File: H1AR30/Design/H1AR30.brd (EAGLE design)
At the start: 34.6 x 30 mm, 21 parts, among them P1 HEXABIT_17.32_NO_P3, U1 STM32F091CBU6, X1 XTALL_CSTCE8M00G52

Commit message: in this commit: - schematic is done - PCB is done - all output files were generated
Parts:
- added C10: 4.7uF, Hexabitz:C-0805-POL
- added C11, C12, C15: 100nF, Hexabitz:C-0603
- added C13, C14: 47pF, Hexabitz:C-0603
- added C16: 100uF, Hexabitz:C-3225
- added C17: 1uF, Hexabitz:C-0805-POL
- added D2: RED, Hexabitz:VLMS1300-GS08
- added D3: GREEN, Hexabitz:VLMS1300-GS08
- added FB2: (no value), Hexabitz:FB-TDK_MMZ1608Y300B
- added PWR: 3-644456-2, Hexabitz:TE_3-644456-2
- added R4, R5: 27.0Ω, Hexabitz:R-0603
- added R6: 39.0Ω, Hexabitz:R-0603
- added R7: 270.0Ω, Hexabitz:R-0603
- added R8: 4.7kΩ, Hexabitz:R-0603
- added R9: 10kΩ, Hexabitz:R-0603
- added U2: FT230XQ-R, Hexabitz:QFN16
- added U3: LM3940IMP-3.3, Hexabitz:SOT230P696X180-4N
- added USB-B*: 1981568-1, Hexabitz:TE_1981568-1
- C1: value 10nF -> 100nF
- C3: value 100nF -> 4.7uF; device Hexabitz:C-0603 -> Hexabitz:C-0805-POL
- C5: value 100nF -> 10nF
- C7: value 4.7uF -> 100nF; device Hexabitz:C-0805-POL -> Hexabitz:C-0603
- D1: value VLMS1300-GS08 -> RED
- R2: value 0.0R -> 10.0K
- R3: value 10.0K -> 0.0R
- moved C6 15.3 mm to (29.0, 45.0), turned to 90 degrees
- moved C8 14.5 mm to (28.7, 37.9)
- moved C7 13.8 mm to (39.6, 46.4), turned to 180 degrees
- moved D1 13.0 mm to (38.2, 31.2), turned to 180 degrees
- moved R1 12.5 mm to (36.7, 31.3)
- moved R2 12.1 mm to (39.8, 45.4), flipped to the top, turned to 180 degrees
- moved C3 11.5 mm to (26.9, 45.1)
- moved C5 10.5 mm to (40.0, 37.4)
- moved D 10.5 mm to (23.0, 34.7)
- moved C 10.5 mm to (23.0, 37.3)
- moved R3 9.42 mm to (44.1, 37.4), turned to 90 degrees
- moved C1 8.43 mm to (47.0, 37.4), turned to 180 degrees
- moved R 8.11 mm to (46.3, 35.3)
- moved U1 6.35 mm to (33.6, 40.9)
- moved X1 5.87 mm to (40.5, 41.3)
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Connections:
- new net N$1: R1.2, U1.P$16
- new net N$10: FB2.2, PWR.2
- new net N$11: C17.1, FB2.1, U3.1
- new net N$12: R5.2, U2.6
- new net N$13: R4.2, U2.7
- new net N$14: R7.1, U2.5
- new net N$15: R6.1, U2.11
- new net N$16: D2.C, R7.2
- new net N$17: D3.C, R6.2
- new net N$18: PWR.1, R8.2, USB-B*.1
- new net N$2: C14.1, R4.1, USB-B*.2
- new net UART1_CTS: U1.P$32, U2.16
- new net UART1_RTS: U1.P$33, U2.4
- new net VBUS_SENSE: R8.1, R9.2, U2.14
- net B1: now also R2.2; no longer R3.2
- net GND: now also C1.2, C10.2, C11.2, C12.2, C13.2, C14.2, C15.2, C16.1, C17.2, R9.1, U1.P$19, U1.P$27, U1.P$3, U1.P$38, U2.13, U2.17, U2.3, U3.2, U3.4, USB-B*.10, USB-B*.11, USB-B*.5, USB-B*.6, USB-B*.7, USB-B*.8, USB-B*.9; no longer C5.2
- net N$3: now also C13.1, R5.1, USB-B*.3; no longer R1.2, U1.P$32
- net R1: now also C1.1; no longer C8.1
- net UART1_RX: now also U2.15
- net UART1_TX: now also U2.2
- net UART2_RX: now also P1.PAD_PD1
- net UART2_TX: now also P1.PAD_PU1
- net UART3_RX: now also P1.PAD_PD4
- net UART3_TX: now also P1.PAD_PU4
- net UART4_RX: now also P1.PAD_PD5
- net UART4_TX: now also P1.PAD_PU5
- net UART5_RX: now also P1.PAD_PD6
- net UART5_TX: now also P1.PAD_PU6
- net UART6_RX: now also P1.PAD_PD2
- net UART6_TX: now also P1.PAD_PU2
- net VDD: now also C10.1, C11.1, C12.1, C15.1, C16.2, C8.1, D2.A, D3.A, U2.1, U2.10, U2.8, U2.9, U3.3; no longer C5.1
- net VDDA: now also C5.1; no longer C1.1
- net VSSA: now also C5.2, R3.2; no longer C1.2, R2.2
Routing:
- net GND: track 0.00 -> 58.8 mm, vias 0 -> 6
- net VDD: track 0.00 -> 54.1 mm, vias 0 -> 6
- net UART4_RX: track 0.00 -> 26.8 mm, vias 0 -> 2
- net UART4_TX: track 0.00 -> 23.8 mm, vias 0 -> 1
- net UART1_CTS: track 0.00 -> 19.3 mm, vias 0 -> 2
- net UART6_TX: track 0.00 -> 18.7 mm, vias 0 -> 1
- net UART6_RX: track 0.00 -> 18.4 mm
- net UART1_RX: track 0.00 -> 18.2 mm, vias 0 -> 2
- net UART3_TX: track 0.00 -> 17.9 mm, vias 0 -> 1
- net UART3_RX: track 0.00 -> 17.2 mm, vias 0 -> 2
- net N$9: track 0.00 -> 17.1 mm, vias 0 -> 2
- net UART1_RTS: track 0.00 -> 17.1 mm, vias 0 -> 2
- net N$7: track 0.00 -> 15.5 mm, vias 0 -> 1
- net UART1_TX: track 0.00 -> 14.9 mm, vias 0 -> 2
- net UART2_RX: track 0.00 -> 14.8 mm, vias 0 -> 2
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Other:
- board text added: "H1AR20"
- board text removed: "H1AR30"

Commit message: replaced (USB-B*) with (PUSB*) and fixed gerber files
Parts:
- renumbered USB-B* to PUSB*
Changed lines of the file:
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@@
 <drawing>
 <settings>
-<setting alwaysvectorfont="yes"/>
+<setting alwaysvectorfont="no"/>
 <setting verticaltext="up"/>
 </settings>
@@
 <attribute name="VALUE" x="30.8704" y="35.36611875" size="1.016" layer="27" ratio="10" rot="SR0"/>
 </element>
-<element name="USB-B*" library="Hexabitz" package="TE_1981568-1" value="1981568-1" x="34.8615" y="22.7838" smashed="yes">
+<element name="PUSB*" library="Hexabitz" package="TE_1981568-1" value="1981568-1" x="34.8615" y="22.7838" smashed="yes">
 <attribute name="DESCRIPTION" value=" USB - micro B USB 2.0 Receptacle Connector 5 Position Surface Mount, Right Angle " x="34.8615" y="22.7838" size="1.778" layer="27" display="off"/>
 <attribute name="MFN" value="TE Connectivity" x="34.8615" y="22.7838" size="1.778" layer="27" display="off"/>
@@
 <wire x1="33.6644625" y1="40.0685" x2="31.544" y2="42.1889625" width="0.254" layer="1"/>
 <wire x1="31.544" y1="42.9641" x2="31.544" y2="42.1889625" width="0.254" layer="1"/>
-<contactref element="USB-B*" pad="5"/>
-<contactref element="USB-B*" pad="11"/>
-<contactref element="USB-B*" pad="6"/>
-<contactref element="USB-B*" pad="10"/>
-<contactref element="USB-B*" pad="7"/>
-<contactref element="USB-B*" pad="9"/>
-<contactref element="USB-B*" pad="8"/>
+<contactref element="PUSB*" pad="5"/>
+<contactref element="PUSB*" pad="11"/>
+<contactref element="PUSB*" pad="6"/>
+<contactref element="PUSB*" pad="10"/>
+<contactref element="PUSB*" pad="7"/>
+<contactref element="PUSB*" pad="9"/>
+<contactref element="PUSB*" pad="8"/>
 <wire x1="36.1615" y1="25.4588" x2="37.8365" y2="25.4588" width="0.254" layer="1"/>
 <wire x1="37.8365" y1="25.4588" x2="38.0615" y2="25.2338" width="0.254" layer="1"/>
@@
 <contactref element="C14" pad="1"/>
 <contactref element="R4" pad="1"/>
-<contactref element="USB-B*" pad="2"/>
+<contactref element="PUSB*" pad="2"/>
 <wire x1="33.4645" y1="22.1352" x2="33.4527" y2="22.147" width="0.254" layer="16"/>
 <wire x1="33.4527" y1="22.147" x2="33.4527" y2="23.8887" width="0.254" layer="16"/>
@@
 <contactref element="R5" pad="1"/>
 <wire x1="36.9706" y1="22.3647" x2="36.9824" y2="22.3765" width="0.254" layer="16"/>
-<contactref element="USB-B*" pad="3"/>
+<contactref element="PUSB*" pad="3"/>
 <wire x1="39.7256" y1="23.5994" x2="39.2585" y2="24.0665" width="0.254" layer="1"/>
 <via x="39.7256" y="23.5994" extent="1-16" drill="0.35"/>
@@
 <wire x1="28.321" y1="30.353" x2="27.1272" y2="31.5468" width="0.254" layer="16"/>
 <wire x1="27.1272" y1="31.5468" x2="27.1272" y2="32.0675" width="0.254" layer="16"/>
-<contactref element="USB-B*" pad="1"/>
+<contactref element="PUSB*" pad="1"/>
 <wire x1="33.5615" y1="25.4588" x2="33.5615" y2="27.8176" width="0.254" layer="1"/>
 <wire x1="32.8284" y1="28.5507" x2="32.0929" y2="28.5507" width="0.254" layer="1"/>

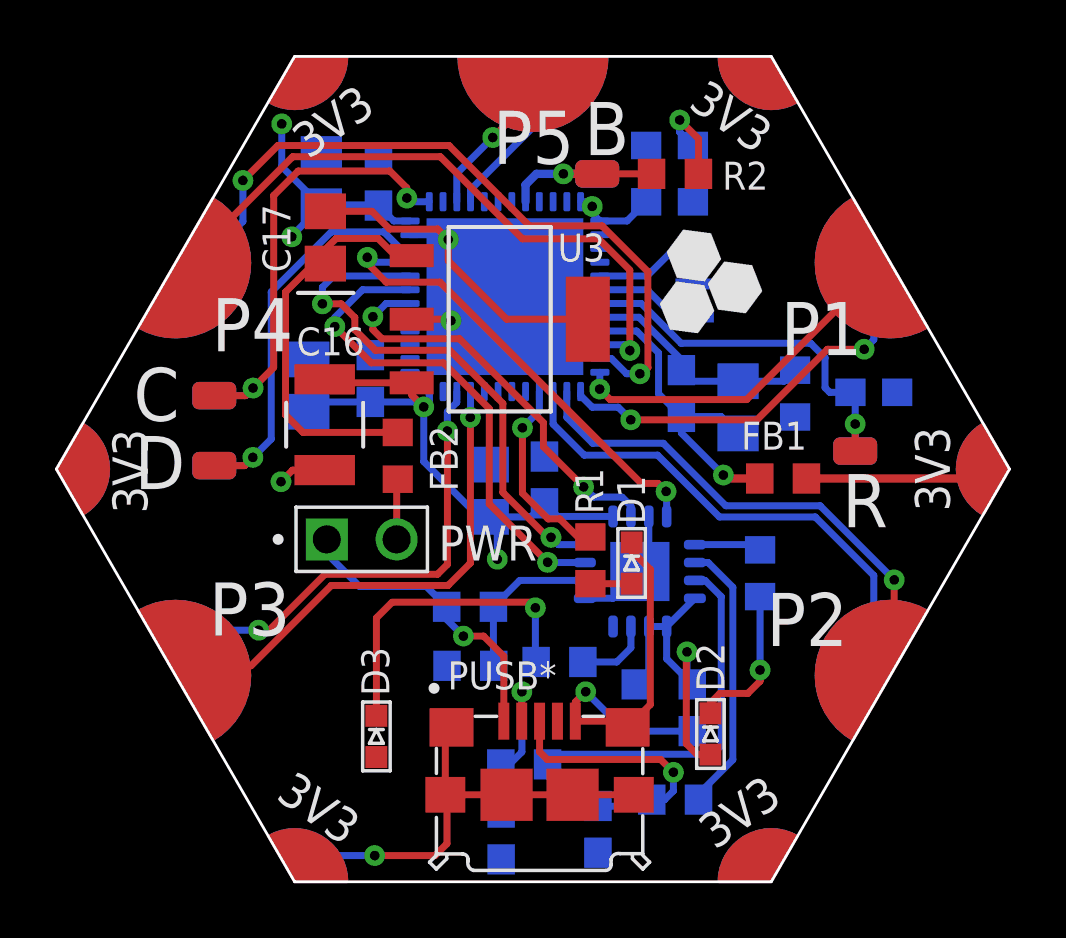
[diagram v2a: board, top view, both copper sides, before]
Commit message: Fix PN and move it a bit. Minor trace update Regenerate gerber and pick n place
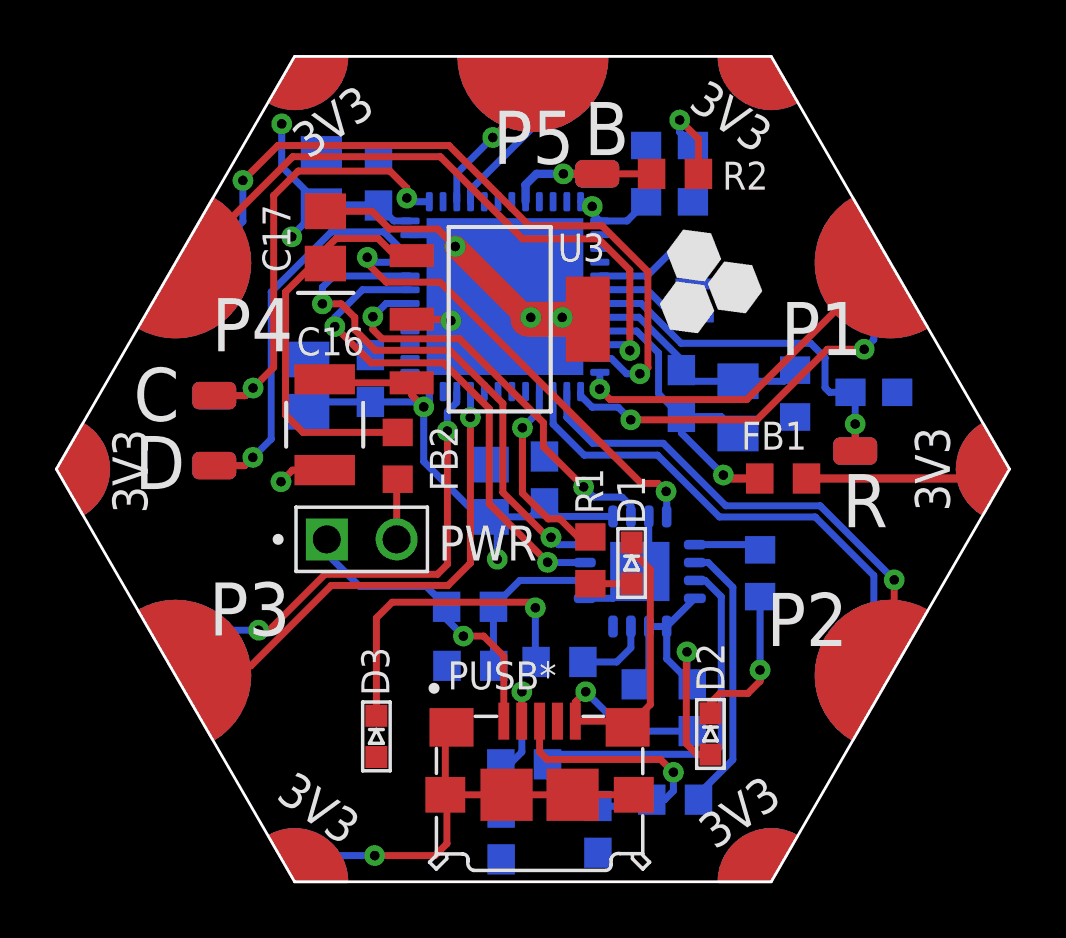
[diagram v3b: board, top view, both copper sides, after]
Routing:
- net GND: track 58.8 -> 58.4 mm, vias 6 -> 8
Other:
- board text added: "H1AR30"
- board text removed: "H1AR20"
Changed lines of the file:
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@@
 <drawing>
 <settings>
-<setting alwaysvectorfont="no"/>
+<setting alwaysvectorfont="yes"/>
 <setting verticaltext="up"/>
 </settings>
-<grid distance="0.5" unitdist="mil" unit="mil" style="lines" multiple="1" display="yes" altdistance="5" altunitdist="mil" altunit="mil"/>
+<grid distance="5" unitdist="mil" unit="mil" style="lines" multiple="1" display="yes" altdistance="5" altunitdist="mil" altunit="mil"/>
 <layers>
 <layer number="1" name="Top" color="4" fill="1" visible="yes" active="yes"/>
@@
 <text x="34.6454" y="46.6784" size="1.9304" layer="21" font="vector" align="center">P5</text>
 <text x="34.5311" y="46.6911" size="1.9304" layer="22" font="vector" rot="MR0" align="center">P5</text>
-<text x="28.2194" y="24.106125" size="1.6764" layer="22" font="vector" rot="MR0" align="center">H1AR20</text>
+<text x="28.1813" y="25.299925" size="1.6764" layer="22" font="vector" rot="MR0" align="center">H1AR30</text>
 <rectangle x1="40.60316875" y1="39.551103125" x2="40.6179" y2="39.565834375" layer="21"/>
 <rectangle x1="40.485315625" y1="39.565834375" x2="40.632634375" y2="39.580565625" layer="21"/>
@@
 <wire x1="28.768" y1="43.9903" x2="29.4132" y2="43.3451" width="0.254" layer="1"/>
 <wire x1="29.4132" y1="43.3451" x2="31.163" y2="43.3451" width="0.254" layer="1"/>
-<wire x1="31.163" y1="43.3451" x2="31.544" y2="42.9641" width="0.254" layer="1"/>
-<via x="31.544" y="42.9641" extent="1-16" drill="0.35"/>
-<wire x1="33.602928125" y1="40.88891875" x2="31.352928125" y2="43.13891875" width="0.254" layer="16"/>
-<wire x1="31.352928125" y1="43.13891875" x2="30.152921875" y2="43.13891875" width="0.254" layer="16"/>
+<wire x1="31.163" y1="43.3451" x2="31.798" y2="42.7101" width="0.254" layer="1"/>
+<via x="31.798" y="42.7101" extent="1-16" drill="0.35"/>
+<wire x1="33.602928125" y1="40.88891875" x2="33.602928125" y2="41.01591875" width="0.254" layer="16"/>
+<wire x1="33.602928125" y1="41.01591875" x2="31.479928125" y2="43.13891875" width="0.254" layer="16"/>
+<wire x1="31.479928125" y1="43.13891875" x2="30.152921875" y2="43.13891875" width="0.254" layer="16"/>
 <contactref element="U1" pad="P$3"/>
 <contactref element="U1" pad="P$27"/>
@@
 <wire x1="40.64" y1="46.6217" x2="40.64" y2="45.3574375" width="0.254" layer="1"/>
 <wire x1="40.6335125" y1="45.35095" x2="40.64" y2="45.3574375" width="0.254" layer="1"/>
-<wire x1="36.6141" y1="40.0685" x2="33.6644625" y2="40.0685" width="0.254" layer="1"/>
-<wire x1="33.6644625" y1="40.0685" x2="31.544" y2="42.1889625" width="0.254" layer="1"/>
-<wire x1="31.544" y1="42.9641" x2="31.544" y2="42.1889625" width="0.254" layer="1"/>
+<wire x1="36.6141" y1="40.0685" x2="34.4391625" y2="40.0685" width="1.27" layer="1"/>
+<wire x1="34.4391625" y1="40.0685" x2="31.798" y2="42.7096625" width="0.8128" layer="1"/>
+<wire x1="31.798" y1="42.7101" x2="31.798" y2="42.7096625" width="0.254" layer="1"/>
 <contactref element="PUSB*" pad="5"/>
 <contactref element="PUSB*" pad="11"/>
@@
 <wire x1="36.5064" y1="29.9241" x2="37.5314" y2="29.9241" width="0.254" layer="16"/>
 <wire x1="37.5314" y1="29.9241" x2="38.5064" y2="30.8991" width="0.254" layer="16"/>
+<via x="34.544" y="40.132" extent="1-16" drill="0.35"/>
+<via x="35.687" y="40.132" extent="1-16" drill="0.35"/>
 </signal>
 <signal name="VDD">

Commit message: changed LED's colors, updated BOM and PDF schematic
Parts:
- D2: value RED -> YELLOW
- D3: value GREEN -> ORANGE
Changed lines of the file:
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@@
 <drawing>
 <settings>
-<setting alwaysvectorfont="yes"/>
+<setting alwaysvectorfont="no"/>
 <setting verticaltext="up"/>
 </settings>
@@
 <attribute name="VALUE" x="37.123371875" y="25.719784375" size="1.016" layer="28" rot="MR0"/>
 </element>
-<element name="D2" library="Hexabitz" package="VLMS1300-GS08" value="RED" x="41.0718" y="24.9936" smashed="yes" rot="R180">
+<element name="D2" library="Hexabitz" package="VLMS1300-GS08" value="YELLOW" x="41.0718" y="24.9936" smashed="yes" rot="R180">
 <attribute name="MFN" value="Vishay" x="41.0718" y="24.9936" size="1.778" layer="27" rot="R180" display="off"/>
-<attribute name="MPN" value="VLMS1300-GS08" x="41.0718" y="24.9936" size="1.778" layer="27" rot="R180" display="off"/>
+<attribute name="MPN" value="VLMY1300-GS08" x="41.0718" y="24.9936" size="1.778" layer="27" rot="R180" display="off"/>
 <attribute name="NAME" x="41.5784" y="26.5369" size="1.016" layer="25" rot="R90"/>
-<attribute name="OCTOPART_URL" value="https://octopart.com/vlms1300-gs08-vishay-21709201?r=sp&amp;s=0nXJNjGsSbWwqfqWlZv0EA" x="41.0718" y="24.9936" size="1.778" layer="27" rot="R180" display="off"/>
+<attribute name="OCTOPART_URL" value="https://octopart.com/vlmy1300-gs08-vishay-21709204?r=sp" x="41.0718" y="24.9936" size="1.778" layer="27" rot="R180" display="off"/>
 <attribute name="VALUE" x="43.0718" y="27.8686" size="1.016" layer="27" rot="R180"/>
 </element>
-<element name="D3" library="Hexabitz" package="VLMS1300-GS08" value="GREEN" x="28.9306" y="24.9047" smashed="yes" rot="R180">
+<element name="D3" library="Hexabitz" package="VLMS1300-GS08" value="ORANGE" x="28.9306" y="24.9047" smashed="yes" rot="R180">
 <attribute name="MFN" value="Vishay" x="28.9306" y="24.9047" size="1.778" layer="27" rot="R180" display="off"/>
-<attribute name="MPN" value="VLMTG1300-GS08" x="28.9306" y="24.9047" size="1.778" layer="27" rot="R180" display="off"/>
+<attribute name="MPN" value="VLMO1300-GS08 " x="28.9306" y="24.9047" size="1.778" layer="27" rot="R180" display="off"/>
 <attribute name="NAME" x="29.3991" y="26.3845" size="1.016" layer="25" rot="R90"/>
-<attribute name="OCTOPART_URL" value="https://octopart.com/vlmtg1300-gs08-vishay-21709202" x="28.9306" y="24.9047" size="1.778" layer="27" rot="R180" display="off"/>
+<attribute name="OCTOPART_URL" value="https://octopart.com/vlmo1300-gs08-vishay-21709200?r=sp#" x="28.9306" y="24.9047" size="1.778" layer="27" rot="R180" display="off"/>
 <attribute name="VALUE" x="30.9306" y="27.7797" size="1.016" layer="27" rot="R180"/>
 </element>
